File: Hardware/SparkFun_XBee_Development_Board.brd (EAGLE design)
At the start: 45.7 x 63.5 mm, 150 parts, among them J4 QWIIC_RIGHT_ANGLE, Q2 3.1A/30V/105mΩ, U1 FSUSB30MUX_MSOP10, U2 AP63203, U3 ESD Diode, U4 MCP73831, U5 ESD Diode, U7 FT231XS

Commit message: Fixes the order of the capacitors
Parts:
- moved C7 1.52 mm to (18.3, 43.3)
- moved C9 1.52 mm to (19.8, 43.3)
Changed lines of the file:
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@@
 <layer number="37" name="tTest" color="7" fill="1" visible="no" active="yes"/>
 <layer number="38" name="bTest" color="7" fill="1" visible="no" active="yes"/>
-<layer number="39" name="tKeepout" color="4" fill="11" visible="no" active="yes"/>
+<layer number="39" name="tKeepout" color="4" fill="11" visible="yes" active="yes"/>
 <layer number="40" name="bKeepout" color="1" fill="11" visible="no" active="yes"/>
 <layer number="41" name="tRestrict" color="4" fill="10" visible="no" active="yes"/>
@@
 <attribute name="VALUE" x="4.826" y="36.322" size="0.6096" layer="27" font="vector" ratio="20" rot="R180" align="top-center"/>
 </element>
-<element name="C7" library="SparkFun-Capacitors" package="0603" value="10nF" x="19.812" y="43.307" smashed="yes" rot="R270">
+<element name="C7" library="SparkFun-Capacitors" package="0603" value="10nF" x="18.288" y="43.307" smashed="yes" rot="R270">
+<attribute name="NAME" x="19.05" y="43.307" size="0.6096" layer="25" font="vector" ratio="20" rot="R270" align="bottom-center"/>
+<attribute name="PROD_ID" value="CAP-00867" x="18.288" y="43.307" size="1.778" layer="27" rot="R270" display="off"/>
+<attribute name="VALUE" x="17.526" y="43.307" size="0.6096" layer="27" font="vector" ratio="20" rot="R270" align="top-center"/>
+</element>
+<element name="C9" library="SparkFun-Capacitors" package="0603" value="0.1uF" x="19.812" y="43.307" smashed="yes" rot="R270">
 <attribute name="NAME" x="20.574" y="43.307" size="0.6096" layer="25" font="vector" ratio="20" rot="R270" align="bottom-center"/>
-<attribute name="PROD_ID" value="CAP-00867" x="19.812" y="43.307" size="1.778" layer="27" rot="R270" display="off"/>
+<attribute name="PROD_ID" value="CAP-00810" x="19.812" y="43.307" size="1.778" layer="27" rot="R270" display="off"/>
 <attribute name="VALUE" x="19.05" y="43.307" size="0.6096" layer="27" font="vector" ratio="20" rot="R270" align="top-center"/>
-</element>
-<element name="C9" library="SparkFun-Capacitors" package="0603" value="0.1uF" x="18.288" y="43.307" smashed="yes" rot="R270">
-<attribute name="NAME" x="19.05" y="43.307" size="0.6096" layer="25" font="vector" ratio="20" rot="R270" align="bottom-center"/>
-<attribute name="PROD_ID" value="CAP-00810" x="18.288" y="43.307" size="1.778" layer="27" rot="R270" display="off"/>
-<attribute name="VALUE" x="17.526" y="43.307" size="0.6096" layer="27" font="vector" ratio="20" rot="R270" align="top-center"/>
 </element>
 <element name="C10" library="SparkFun-Capacitors" package="0603" value="10uF" x="21.336" y="43.307" smashed="yes" rot="R270">
@@
 <wire x1="22.567" y1="44.157" x2="22.606" y2="44.196" width="0.762" layer="1"/>
 <via x="22.606" y="44.196" extent="1-16" drill="0.3048"/>
-<wire x1="21.336" y1="44.157" x2="19.812" y2="44.157" width="0.762" layer="1"/>
-<wire x1="19.812" y1="44.157" x2="18.288" y2="44.157" width="0.762" layer="1"/>
-<wire x1="18.288" y1="44.157" x2="16.764" y2="44.157" width="0.762" layer="1"/>
+<wire x1="21.336" y1="44.157" x2="21.2852" y2="44.1062" width="0.762" layer="1"/>
 <wire x1="16.764" y1="44.157" x2="15.24" y2="44.157" width="0.762" layer="1"/>
 <contactref element="C14" pad="1"/>
@@
 <contactref element="U7" pad="13"/>
 <contactref element="L1" pad="P$2"/>
+<wire x1="21.336" y1="44.157" x2="19.812" y2="44.157" width="0.762" layer="1"/>
+<wire x1="19.812" y1="44.157" x2="18.288" y2="44.157" width="0.762" layer="1"/>
+<wire x1="18.288" y1="44.157" x2="16.764" y2="44.157" width="0.762" layer="1"/>
+<wire x1="29.9466" y1="40.259" x2="30.7594" y2="40.259" width="0" layer="19" extent="1-1"/>
+<wire x1="30.221" y1="36.957" x2="29.9466" y2="40.259" width="0" layer="19" extent="1-1"/>
+<wire x1="30.48" y1="34.163" x2="30.221" y2="36.957" width="0" layer="19" extent="1-1"/>
+<wire x1="30.48" y1="33.274" x2="30.48" y2="34.163" width="0" layer="19" extent="1-1"/>
+<wire x1="30.48" y1="32.258" x2="30.48" y2="33.274" width="0" layer="19" extent="1-1"/>
+<wire x1="29.298" y1="33.401" x2="30.48" y2="33.274" width="0" layer="19" extent="1-1"/>
+<wire x1="29.298" y1="31.9024" x2="30.48" y2="32.258" width="0" layer="19" extent="1-1"/>
+<wire x1="22.5806" y1="37.8206" x2="30.221" y2="36.957" width="0" layer="19" extent="1-1"/>
+<wire x1="21.2852" y1="44.1062" x2="21.4849" y2="37.78" width="0" layer="19" extent="1-1"/>
+<wire x1="7.62" y1="44.45" x2="10.36" y2="44.13" width="0" layer="19" extent="1-1"/>
+<wire x1="33.147" y1="23.114" x2="30.48" y2="32.258" width="0" layer="19" extent="1-1"/>
+<wire x1="33.108" y1="21.971" x2="33.147" y2="23.114" width="0" layer="19" extent="1-1"/>
+<wire x1="33.3375" y1="20.4597" x2="33.108" y2="21.971" width="0" layer="19" extent="1-1"/>
+<wire x1="31.4325" y1="15.1003" x2="33.3375" y2="20.4597" width="0" layer="19" extent="1-1"/>
+<wire x1="30.7975" y1="15.1003" x2="31.4325" y2="15.1003" width="0" layer="19" extent="1-1"/>
+<wire x1="30.1625" y1="15.1003" x2="30.7975" y2="15.1003" width="0" layer="19" extent="1-1"/>
+<wire x1="31.662" y1="13.589" x2="31.4325" y2="15.1003" width="0" layer="19" extent="1-1"/>
+<wire x1="30.48" y1="13.589" x2="31.662" y2="13.589" width="0" layer="19" extent="1-1"/>
+<wire x1="41.91" y1="16.256" x2="33.3375" y2="20.4597" width="0" layer="19" extent="1-16"/>
+<wire x1="41.791" y1="9.66" x2="41.91" y2="16.256" width="0" layer="19" extent="16-16"/>
+<wire x1="13.12" y1="17.78" x2="30.1625" y2="15.1003" width="0" layer="19" extent="1-1"/>
+<wire x1="13.12" y1="19.304" x2="13.12" y2="17.78" width="0" layer="19" extent="1-1"/>
+<wire x1="13.081" y1="20.447" x2="13.12" y2="19.304" width="0" layer="19" extent="1-1"/>
+<wire x1="5.842" y1="20.8788" x2="13.081" y2="20.447" width="0" layer="19" extent="1-1"/>
+<wire x1="1.27" y1="20.955" x2="5.842" y2="20.8788" width="0" layer="19" extent="1-1"/>
 </signal>
 <signal name="V_USB">

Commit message: Updates production panel
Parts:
- moved U$36 0.08 mm to (20.8, 3.38)
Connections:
- net RLED1 renamed IOLED
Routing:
- net VIN: track 25.0 -> 24.4 mm
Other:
- board text added: "1oz Outer Layer 0.5oz Inner Layer JLC0416H-7628 Stackup"
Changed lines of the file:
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@@
 <layer number="37" name="tTest" color="7" fill="1" visible="no" active="yes"/>
 <layer number="38" name="bTest" color="7" fill="1" visible="no" active="yes"/>
-<layer number="39" name="tKeepout" color="4" fill="11" visible="yes" active="yes"/>
+<layer number="39" name="tKeepout" color="4" fill="11" visible="no" active="yes"/>
 <layer number="40" name="bKeepout" color="1" fill="11" visible="no" active="yes"/>
 <layer number="41" name="tRestrict" color="4" fill="10" visible="no" active="yes"/>
@@
 <layer number="115" name="ReferenceISLANDS" color="7" fill="1" visible="no" active="yes"/>
 <layer number="116" name="Patch_BOT" color="9" fill="4" visible="no" active="yes"/>
-<layer number="117" name="PM_Ref" color="26" fill="1" visible="no" active="yes"/>
+<layer number="117" name="PM_Ref" color="26" fill="1" visible="yes" active="yes"/>
 <layer number="118" name="Rect_Pads" color="7" fill="1" visible="no" active="yes"/>
-<layer number="119" name="PF_Ref" color="31" fill="1" visible="no" active="yes"/>
-<layer number="120" name="WFL_Ref" color="25" fill="1" visible="no" active="yes"/>
+<layer number="119" name="PF_Ref" color="31" fill="1" visible="yes" active="yes"/>
+<layer number="120" name="WFL_Ref" color="25" fill="1" visible="yes" active="yes"/>
 <layer number="121" name="_tsilk" color="7" fill="1" visible="no" active="yes"/>
 <layer number="122" name="_bsilk" color="7" fill="1" visible="no" active="yes"/>
@@
 <rectangle x1="27.559" y1="40.513" x2="29.083" y2="40.767" layer="41"/>
 <rectangle x1="27.686" y1="34.671" x2="28.956" y2="34.925" layer="41"/>
+<text x="72.39" y="35.56" size="1.778" layer="51" font="vector" ratio="15">1oz Outer Layer
+0.5oz Inner Layer
+JLC0416H-7628 Stackup</text>
 </plain>
 <attributes>
@@
 </element>
 <element name="U$19" library="pot" package="CHG47" value="" x="25.146" y="16.002" smashed="yes"/>
-<element name="U$33" library="pot" package="IO46" value="" x="5.207" y="5.969" smashed="yes"/>
+<element name="U$33" library="pot" package="IO46" value="" x="5.1816" y="5.9944" smashed="yes"/>
 <element name="U$35" library="top" package="#SHLD#740" value="" x="31.877" y="3.556" smashed="yes" rot="MR0"/>
-<element name="U$36" library="top" package="#SHLD1#741" value="" x="20.828" y="3.302" smashed="yes" rot="MR0"/>
+<element name="U$36" library="top" package="#SHLD1#741" value="" x="20.828" y="3.3782" smashed="yes" rot="MR0"/>
 <element name="U$59" library="top" package="#IOLED#23" value="" x="6.223" y="7.366" smashed="yes" rot="MR0"/>
 </elements>
@@
 <via x="44.45" y="20.32" extent="1-16" drill="0.3048"/>
 <via x="44.45" y="14.097" extent="1-16" drill="0.3048"/>
-<via x="22.86" y="3.81" extent="1-16" drill="0.3048"/>
+<via x="24.0538" y="3.302" extent="1-16" drill="0.3048"/>
 <via x="1.27" y="26.67" extent="1-16" drill="0.3048"/>
 <via x="36.576" y="41.275" extent="1-16" drill="0.3048"/>
@@
 <wire x1="22.567" y1="44.157" x2="22.606" y2="44.196" width="0.762" layer="1"/>
 <via x="22.606" y="44.196" extent="1-16" drill="0.3048"/>
-<wire x1="21.336" y1="44.157" x2="21.2852" y2="44.1062" width="0.762" layer="1"/>
 <wire x1="16.764" y1="44.157" x2="15.24" y2="44.157" width="0.762" layer="1"/>
 <contactref element="C14" pad="1"/>
@@
 <wire x1="19.812" y1="44.157" x2="18.288" y2="44.157" width="0.762" layer="1"/>
 <wire x1="18.288" y1="44.157" x2="16.764" y2="44.157" width="0.762" layer="1"/>
-<wire x1="29.9466" y1="40.259" x2="30.7594" y2="40.259" width="0" layer="19" extent="1-1"/>
-<wire x1="30.221" y1="36.957" x2="29.9466" y2="40.259" width="0" layer="19" extent="1-1"/>
-<wire x1="30.48" y1="34.163" x2="30.221" y2="36.957" width="0" layer="19" extent="1-1"/>
-<wire x1="30.48" y1="33.274" x2="30.48" y2="34.163" width="0" layer="19" extent="1-1"/>
-<wire x1="30.48" y1="32.258" x2="30.48" y2="33.274" width="0" layer="19" extent="1-1"/>
-<wire x1="29.298" y1="33.401" x2="30.48" y2="33.274" width="0" layer="19" extent="1-1"/>
-<wire x1="29.298" y1="31.9024" x2="30.48" y2="32.258" width="0" layer="19" extent="1-1"/>
-<wire x1="22.5806" y1="37.8206" x2="30.221" y2="36.957" width="0" layer="19" extent="1-1"/>
-<wire x1="21.2852" y1="44.1062" x2="21.4849" y2="37.78" width="0" layer="19" extent="1-1"/>
-<wire x1="7.62" y1="44.45" x2="10.36" y2="44.13" width="0" layer="19" extent="1-1"/>
-<wire x1="33.147" y1="23.114" x2="30.48" y2="32.258" width="0" layer="19" extent="1-1"/>
-<wire x1="33.108" y1="21.971" x2="33.147" y2="23.114" width="0" layer="19" extent="1-1"/>
-<wire x1="33.3375" y1="20.4597" x2="33.108" y2="21.971" width="0" layer="19" extent="1-1"/>
-<wire x1="31.4325" y1="15.1003" x2="33.3375" y2="20.4597" width="0" layer="19" extent="1-1"/>
-<wire x1="30.7975" y1="15.1003" x2="31.4325" y2="15.1003" width="0" layer="19" extent="1-1"/>
-<wire x1="30.1625" y1="15.1003" x2="30.7975" y2="15.1003" width="0" layer="19" extent="1-1"/>
-<wire x1="31.662" y1="13.589" x2="31.4325" y2="15.1003" width="0" layer="19" extent="1-1"/>
-<wire x1="30.48" y1="13.589" x2="31.662" y2="13.589" width="0" layer="19" extent="1-1"/>
-<wire x1="41.91" y1="16.256" x2="33.3375" y2="20.4597" width="0" layer="19" extent="1-16"/>
-<wire x1="41.791" y1="9.66" x2="41.91" y2="16.256" width="0" layer="19" extent="16-16"/>
-<wire x1="13.12" y1="17.78" x2="30.1625" y2="15.1003" width="0" layer="19" extent="1-1"/>
-<wire x1="13.12" y1="19.304" x2="13.12" y2="17.78" width="0" layer="19" extent="1-1"/>
-<wire x1="13.081" y1="20.447" x2="13.12" y2="19.304" width="0" layer="19" extent="1-1"/>
-<wire x1="5.842" y1="20.8788" x2="13.081" y2="20.447" width="0" layer="19" extent="1-1"/>
-<wire x1="1.27" y1="20.955" x2="5.842" y2="20.8788" width="0" layer="19" extent="1-1"/>
 </signal>
 <signal name="V_USB">
@@
 <vertex x="20.828" y="22.733"/>
 </polygon>
-<via x="23.114" y="24.257" extent="1-16" drill="0.3048"/>
+<via x="23.0124" y="23.9776" extent="1-16" drill="0.3048"/>
 <contactref element="J9" pad="1"/>
 <wire x1="7.62" y1="19.05" x2="10.033" y2="19.05" width="0.762" layer="15"/>
@@
 <wire x1="10.033" y1="19.05" x2="10.795" y2="19.812" width="0.762" layer="15"/>
 <wire x1="10.795" y1="19.812" x2="10.795" y2="22.225" width="0.762" layer="15"/>
-<wire x1="10.795" y1="22.225" x2="11.811" y2="23.241" width="0.762" layer="15"/>
-<via x="22.86" y="23.241" extent="1-16" drill="0.3048"/>
-<wire x1="11.811" y1="23.241" x2="22.86" y2="23.241" width="0.762" layer="15"/>
-<wire x1="23.114" y1="24.257" x2="23.114" y2="23.495" width="0.762" layer="15"/>
-<wire x1="22.86" y1="23.241" x2="23.114" y2="23.495" width="0.762" layer="15"/>
+<wire x1="10.795" y1="22.225" x2="11.9888" y2="23.4188" width="0.762" layer="15"/>
+<via x="22.4536" y="23.4188" extent="1-16" drill="0.3048"/>
+<wire x1="11.9888" y1="23.4188" x2="22.4536" y2="23.4188" width="0.762" layer="15"/>
+<wire x1="23.0124" y1="23.9776" x2="22.4536" y2="23.4188" width="0.762" layer="15"/>
 <wire x1="21.47" y1="20.835" x2="21.47" y2="22.86" width="0.762" layer="1"/>
 <wire x1="22.86" y1="18.884" x2="24.638" y2="18.884" width="0.762" layer="1"/>
@@
 <wire x1="6.604" y1="8.89" x2="7.024" y2="9.31" width="0.254" layer="1"/>
 </signal>
-<signal name="RLED1">
+<signal name="IOLED">
 <contactref element="IOLED" pad="2"/>
 <contactref element="D8" pad="C"/>
@@
 </drawing>
 <compatibility>
+<note version="6.3" minversion="6.2.2" severity="warning">
+Since Version 6.2.2 text objects can contain more than one line,
+which will not be processed correctly with this version.
+</note>
 <note version="8.3" severity="warning">
 Since Version 8.3, EAGLE supports URNs for individual library

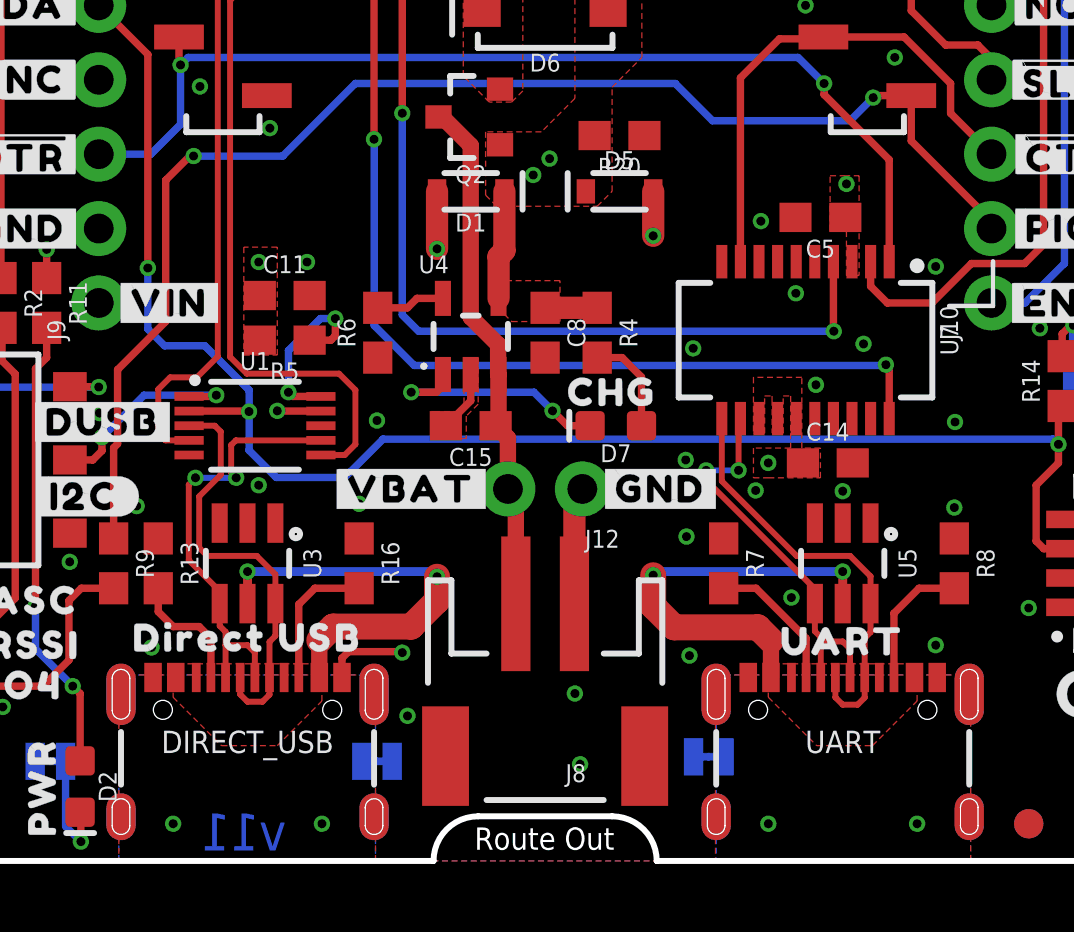
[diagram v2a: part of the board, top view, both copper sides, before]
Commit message: Powers FTDI with VUSB
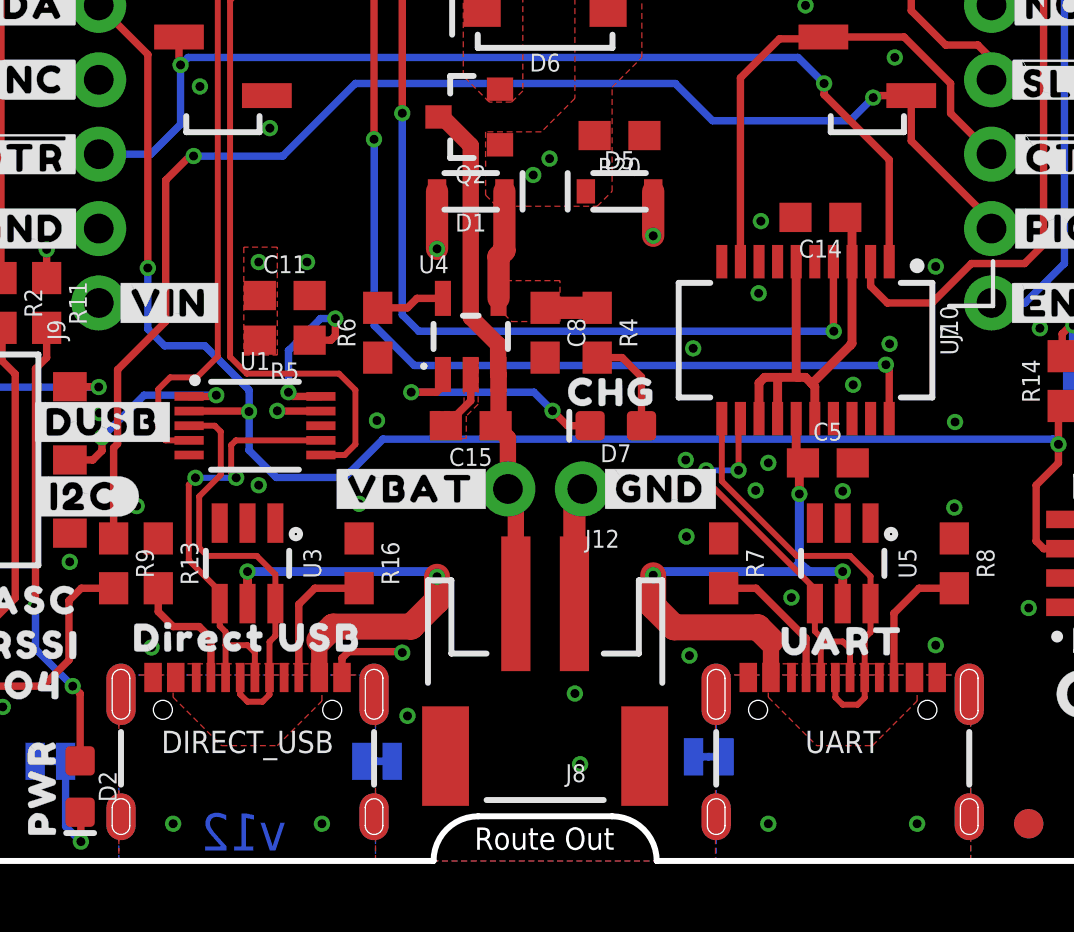
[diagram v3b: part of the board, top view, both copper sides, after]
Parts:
- moved C14 8.39 mm to (32.3, 22.0), turned to 180 degrees
- moved C5 8.39 mm to (32.5, 13.6), turned to 0 degrees
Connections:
- new net N$18: C14.1, U7.13, U7.14, U7.16, U7.3, U7.6
- net 3.3V: no longer C14.1, C5.1, U7.13, U7.14, U7.15, U7.3
- net GND: no longer U7.16, U7.6
- net V_USB: now also C5.1, U7.15
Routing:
- net N$18: track 0.00 -> 16.3 mm
- net V_USB: track 27.6 -> 34.0 mm, vias 3 -> 4
- net 3.3V: vias 14 -> 13
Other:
- board text added: "v12"
- board text removed: "v11"
